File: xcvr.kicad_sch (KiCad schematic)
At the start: 101 parts, among them J103 QBUS_B, Q1 Q_NPN_BCE, Q101 Dual_NMOS, Q102 Dual_NMOS, Q103 Dual_NMOS, Q104 PMOS, Q105 Dual_NMOS, Q106 PMOS, Q2 Dual_NMOS, Q3 Q_NPN_BCE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

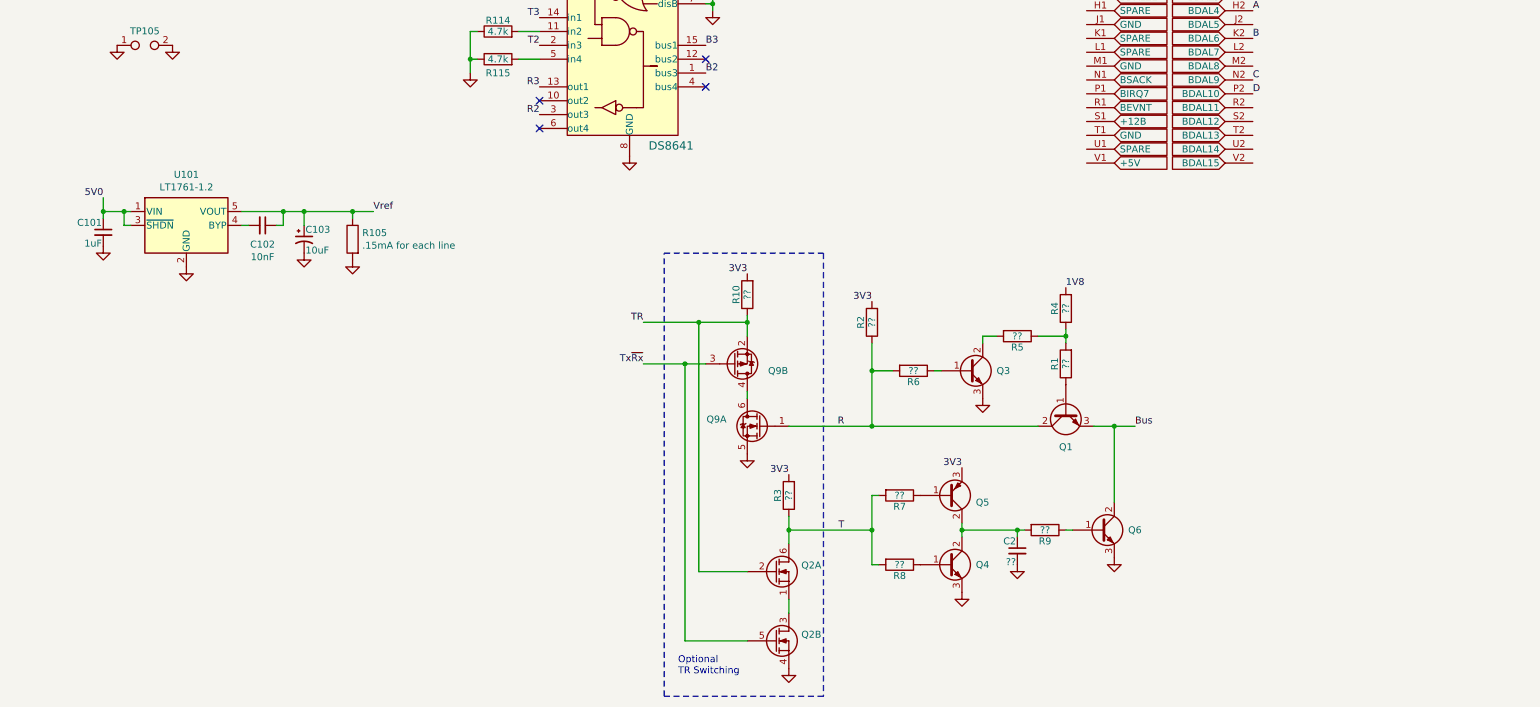
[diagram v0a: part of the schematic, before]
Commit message: Added the discrete comparator circuit
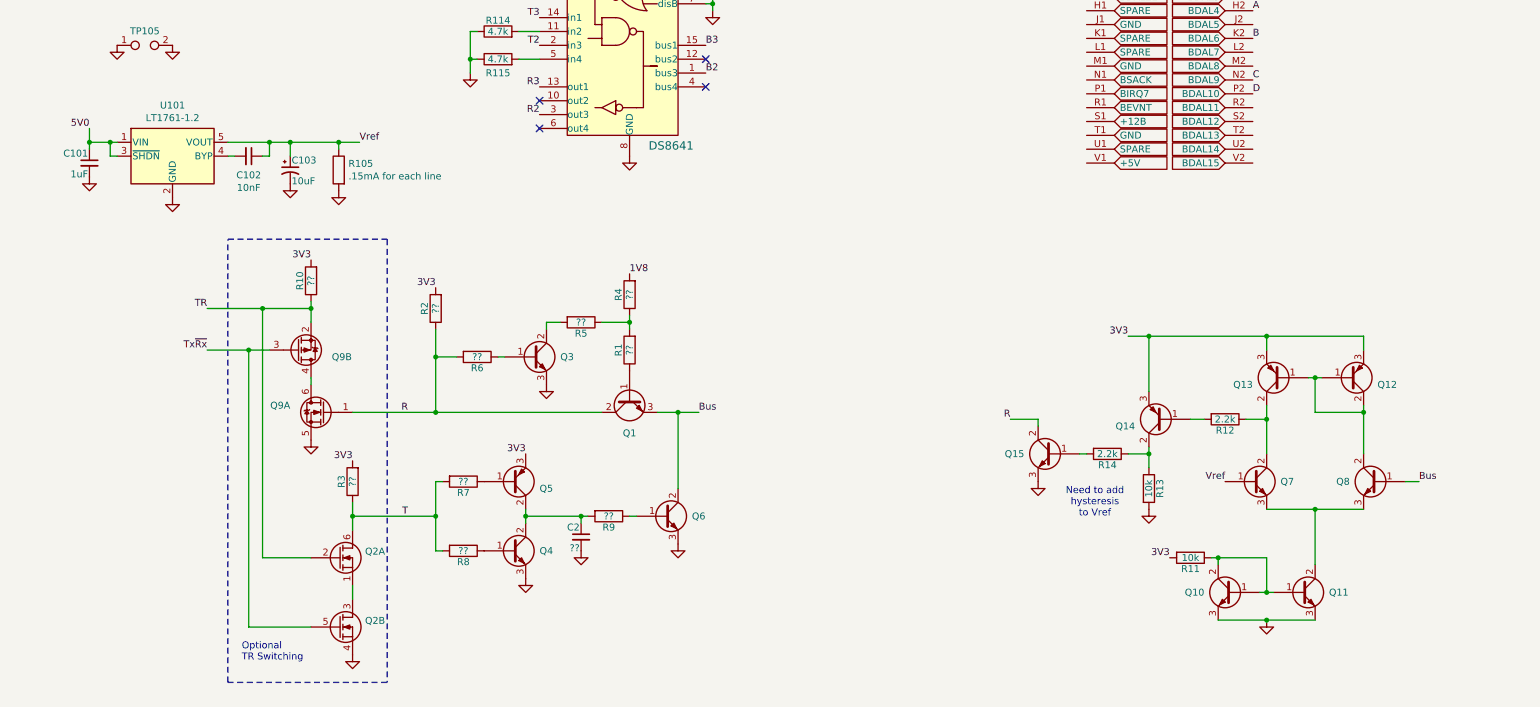
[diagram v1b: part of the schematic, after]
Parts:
- added Q10, Q11, Q15, Q7, Q8: Q_NPN_BCE, symbol Device:Q_NPN_BCE
- added Q12, Q13, Q14: Q_PNP_BCE, symbol Device:Q_PNP_BCE
- added R11, R13: 10k, Resistor_SMD:R_0603_1608Metric, symbol xcvr-rescue:R-xcvr-rescue-xcvr-rescue
- added R12, R14: 2.2k, Resistor_SMD:R_0603_1608Metric, symbol xcvr-rescue:R-xcvr-rescue-xcvr-rescue
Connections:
- net 3V3: now also Q12.3 (E), Q13.3 (E), Q14.3 (E), R11.2
- net Bus: now also Q8.1 (B)
- net GND: now also Q10.3 (E), Q11.3 (E), Q15.3 (E), R13.2
- net R: now also Q15.2 (C)
- net Vref: now also Q7.1 (B)
- new net: Q12.1 (B), Q12.2 (C), Q13.1 (B), Q8.2 (C)
- new net: Q11.2 (C), Q7.3 (E), Q8.3 (E)
- new net: Q10.1 (B), Q10.2 (C), Q11.1 (B), R11.1
- new net: Q13.2 (C), Q7.2 (C), R12.1
- new net: Q14.1 (B), R12.2
- new net: Q15.1 (B), R14.2
- new net: Q14.2 (C), R13.1, R14.1
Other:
- note added: "Need to add hysteresis to Vref"
- moved on the sheet: C101, C102, C103, C2, Q1, Q2A, Q2B, Q3, Q4, Q5, Q6, Q9A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
